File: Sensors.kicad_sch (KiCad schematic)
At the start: 17 parts, among them Q1 TEMT6000X01, U2 BME280, U7 MAX4466EXK

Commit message: setup net classes and started layout
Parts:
- C15, C16, C18, C20: footprint (none) -> Capacitor_SMD:C_0805_2012Metric
- R23, R24, R25, R26, R27, R28, R29, R30, R31: footprint (none) -> Resistor_SMD:R_0805_2012Metric
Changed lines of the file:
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@@
 			)
 		)
-		(property "Footprint" ""
+		(property "Footprint" "Resistor_SMD:R_0805_2012Metric"
 			(at 176.022 109.22 90)
 			(hide yes)
@@
 			)
 		)
-		(property "Footprint" ""
+		(property "Footprint" "Capacitor_SMD:C_0805_2012Metric"
 			(at 227.33 151.4348 0)
 			(hide yes)
@@
 			)
 		)
-		(property "Footprint" ""
+		(property "Footprint" "Resistor_SMD:R_0805_2012Metric"
 			(at 223.52 144.018 90)
 			(hide yes)
@@
 			)
 		)
-		(property "Footprint" ""
+		(property "Footprint" "Resistor_SMD:R_0805_2012Metric"
 			(at 176.022 133.35 90)
 			(hide yes)
@@
 			)
 		)
-		(property "Footprint" ""
+		(property "Footprint" "Capacitor_SMD:C_0805_2012Metric"
 			(at 107.6452 53.34 0)
 			(hide yes)
@@
 			)
 		)
-		(property "Footprint" ""
+		(property "Footprint" "Resistor_SMD:R_0805_2012Metric"
 			(at 43.942 46.99 90)
 			(hide yes)
@@
 			)
 		)
-		(property "Footprint" ""
+		(property "Footprint" "Resistor_SMD:R_0805_2012Metric"
 			(at 188.722 133.35 90)
 			(hide yes)
@@
 			)
 		)
-		(property "Footprint" ""
+		(property "Footprint" "Capacitor_SMD:C_0805_2012Metric"
 			(at 272.7452 115.57 0)
 			(hide yes)
@@
 			)
 		)
-		(property "Footprint" ""
+		(property "Footprint" "Resistor_SMD:R_0805_2012Metric"
 			(at 201.422 44.45 90)
 			(hide yes)
@@
 			)
 		)
-		(property "Footprint" ""
+		(property "Footprint" "Resistor_SMD:R_0805_2012Metric"
 			(at 33.782 46.99 90)
 			(hide yes)
@@
 			)
 		)
-		(property "Footprint" ""
+		(property "Footprint" "Resistor_SMD:R_0805_2012Metric"
 			(at 155.702 114.3 90)
 			(hide yes)
@@
 			)
 		)
-		(property "Footprint" ""
+		(property "Footprint" "Capacitor_SMD:C_0805_2012Metric"
 			(at 151.13 105.7148 0)
 			(hide yes)
@@
 			)
 		)
-		(property "Footprint" ""
+		(property "Footprint" "Resistor_SMD:R_0805_2012Metric"
 			(at 155.702 100.33 90)
 			(hide yes)

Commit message: imported all footprints into layout
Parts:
- MK1: footprint CMC-5042PF-AC:CUI_CMC-5042PF-AC -> ESP32_project_Footprints:CUI_CMC-5042PF-AC; Availability In Stock -> (none); Package None -> (none); Price None -> (none)
- Q1: footprint TEMT6000X01:TRANS_TEMT6000X01 -> ESP32_project_Footprints:TRANS_TEMT6000X01; Availability In Stock -> (none); Package 1206 Vishay -> (none); Price None -> (none)
- U2: footprint BME280:PSON65P250X250X100-8N -> ESP32_project_Footprints:PSON65P250X250X100-8N; Availability In Stock -> (none); Package LGA-8 Bosch -> (none); Price None -> (none)
- U7: footprint MAX4466EXK:SOT65P210X110-5N -> ESP32_project_Footprints:SOT65P210X110-5N; Availability In Stock -> (none); Package SC-70-5 Maxim -> (none); Price None -> (none)
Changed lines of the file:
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@@
 			)
 		)
-		(property "Footprint" "TEMT6000X01:TRANS_TEMT6000X01"
+		(property "Footprint" "ESP32_project_Footprints:TRANS_TEMT6000X01"
 			(at 189.23 53.34 0)
 			(hide yes)
@@
 			)
 		)
-		(property "Package" "1206 Vishay"
-			(at 189.23 53.34 0)
-			(hide yes)
-			(show_name no)
-			(do_not_autoplace no)
-			(effects
-				(font
-					(size 1.27 1.27)
-				)
-				(justify bottom)
-			)
-		)
-		(property "Price" "None"
-			(at 189.23 53.34 0)
-			(hide yes)
-			(show_name no)
-			(do_not_autoplace no)
-			(effects
-				(font
-					(size 1.27 1.27)
-				)
-				(justify bottom)
-			)
-		)
 		(property "Check_prices" "https://www.snapeda.com/parts/TEMT6000X01/Vishay+Semiconductor+Opto+Division/view-part/?ref=eda"
 			(at 189.23 53.34 0)
@@
 		)
 		(property "MP" "TEMT6000X01"
-			(at 189.23 53.34 0)
-			(hide yes)
-			(show_name no)
-			(do_not_autoplace no)
-			(effects
-				(font
-					(size 1.27 1.27)
-				)
-				(justify bottom)
-			)
-		)
-		(property "Availability" "In Stock"
 			(at 189.23 53.34 0)
 			(hide yes)
@@
 			)
 		)
-		(property "Footprint" "CMC-5042PF-AC:CUI_CMC-5042PF-AC"
+		(property "Footprint" "ESP32_project_Footprints:CUI_CMC-5042PF-AC"
 			(at 142.24 125.73 0)
 			(hide yes)
@@
 			)
 		)
-		(property "Package" "None"
-			(at 142.24 125.73 0)
-			(hide yes)
-			(show_name no)
-			(do_not_autoplace no)
-			(effects
-				(font
-					(size 1.27 1.27)
-				)
-				(justify bottom)
-			)
-		)
-		(property "Price" "None"
-			(at 142.24 125.73 0)
-			(hide yes)
-			(show_name no)
-			(do_not_autoplace no)
-			(effects
-				(font
-					(size 1.27 1.27)
-				)
-				(justify bottom)
-			)
-		)
 		(property "Check_prices" "https://www.snapeda.com/parts/CMC-5042PF-AC/Same+Sky/view-part/?ref=eda"
 			(at 142.24 125.73 0)
@@
 			)
 		)
-		(property "Availability" "In Stock"
-			(at 142.24 125.73 0)
-			(hide yes)
-			(show_name no)
-			(do_not_autoplace no)
-			(effects
-				(font
-					(size 1.27 1.27)
-				)
-				(justify bottom)
-			)
-		)
 		(property "MANUFACTURER" "CUI INC"
 			(at 142.24 125.73 0)
@@
 				)
 				(justify bottom)
+			)
+		)
+		(property "Purpose" ""
+			(at 142.24 125.73 0)
+			(show_name no)
+			(do_not_autoplace no)
+			(effects
+				(font
+					(size 1.27 1.27)
+				)
 			)
 		)
@@
 			)
 		)
-		(property "Footprint" "MAX4466EXK:SOT65P210X110-5N"
+		(property "Footprint" "ESP32_project_Footprints:SOT65P210X110-5N"
 			(at 226.06 121.92 0)
 			(hide yes)
@@
 			)
 		)
-		(property "Package" "SC-70-5 Maxim"
-			(at 226.06 121.92 0)
-			(hide yes)
-			(show_name no)
-			(do_not_autoplace no)
-			(effects
-				(font
-					(size 1.27 1.27)
-				)
-				(justify bottom)
-			)
-		)
-		(property "Price" "None"
-			(at 226.06 121.92 0)
-			(hide yes)
-			(show_name no)
-			(do_not_autoplace no)
-			(effects
-				(font
-					(size 1.27 1.27)
-				)
-				(justify bottom)
-			)
-		)
 		(property "SnapEDA_Link" "https://www.snapeda.com/parts/MAX4466EXK/Analog+Devices/view-part/?ref=snap"
 			(at 226.06 121.92 0)
@@
 		)
 		(property "MP" "MAX4466EXK"
-			(at 226.06 121.92 0)
-			(hide yes)
-			(show_name no)
-			(do_not_autoplace no)
-			(effects
-				(font
-					(size 1.27 1.27)
-				)
-				(justify bottom)
-			)
-		)
-		(property "Availability" "In Stock"
 			(at 226.06 121.92 0)
 			(hide yes)
@@
 			)
 		)
-		(property "Footprint" "BME280:PSON65P250X250X100-8N"
+		(property "Footprint" "ESP32_project_Footprints:PSON65P250X250X100-8N"
 			(at 76.2 57.15 0)
 			(hide yes)
@@
 			)
 		)
-		(property "Package" "LGA-8 Bosch"
-			(at 76.2 57.15 0)
-			(hide yes)
-			(show_name no)
-			(do_not_autoplace no)
-			(effects
-				(font
-					(size 1.27 1.27)
-				)
-				(justify bottom)
-			)
-		)
 		(property "Check_prices" "https://www.snapeda.com/parts/BME280/Bosch+Sensortec/view-part/?ref=eda"
 			(at 76.2 57.15 0)
@@
 			(at 76.2 57.15 0)
 			(hide yes)
-			(show_name no)
-			(do_not_autoplace no)
-			(effects
-				(font
-					(size 1.27 1.27)
-				)
-				(justify bottom)
-			)
-		)
-		(property "Price" "None"
-			(at 76.2 57.15 0)
-			(hide yes)
-			(show_name no)
-			(do_not_autoplace no)
-			(effects
-				(font
-					(size 1.27 1.27)
-				)
-				(justify bottom)
-			)
-		)
-		(property "Availability" "In Stock"
-			(at 76.2 57.15 0)
-			(hide yes)

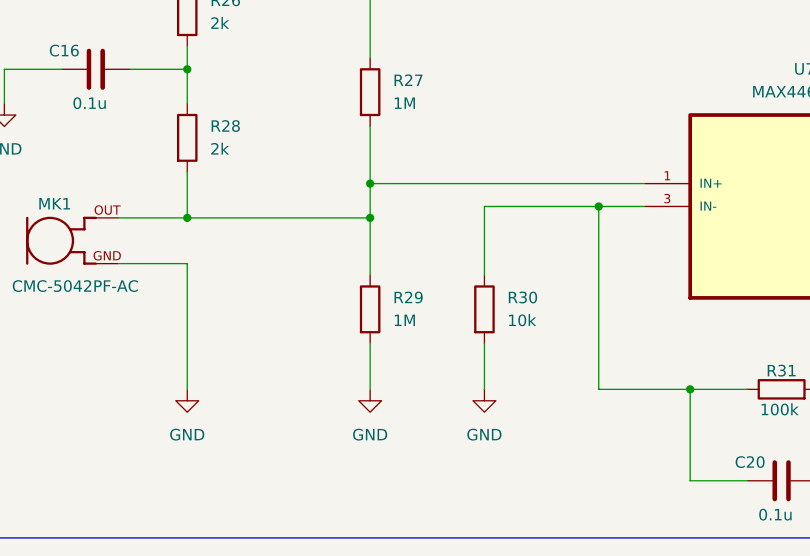
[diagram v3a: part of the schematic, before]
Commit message: finalized edge cuts and component placement
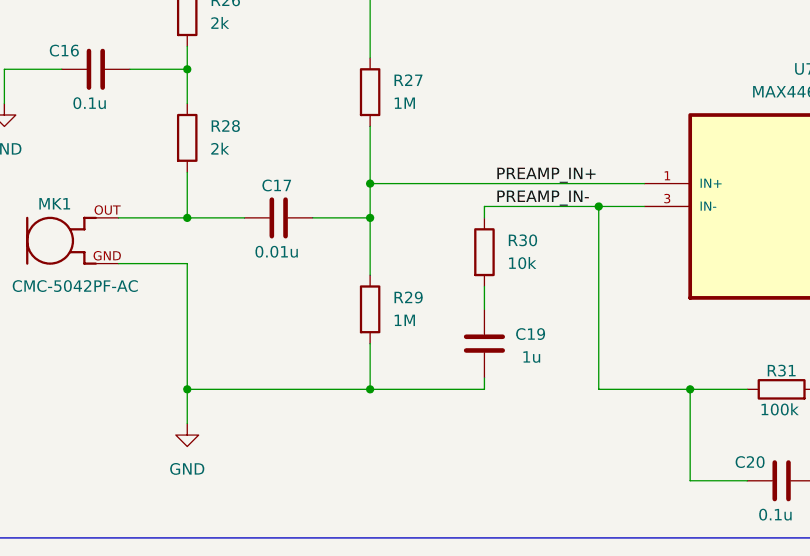
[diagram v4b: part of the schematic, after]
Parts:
- added C17: 0.01u, Capacitor_SMD:C_0805_2012Metric, symbol Device:C
- added C19: 1u, Capacitor_SMD:C_0805_2012Metric, symbol Device:C
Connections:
- net GND: now also C19.1; no longer R30.2
- net PREAMP_IN+: now reaches R27.2, R29.1, U7.1 (IN+)
- net PREAMP_IN+: now also C17.2; no longer MK1.OUT, R28.2
- net PREAMP_IN-: now reaches C20.1, R30.1, R31.1, U7.3 (IN-)
- new net: C17.1, MK1.OUT, R28.2
- new net: C19.2, R30.2
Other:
- moved on the sheet: R30

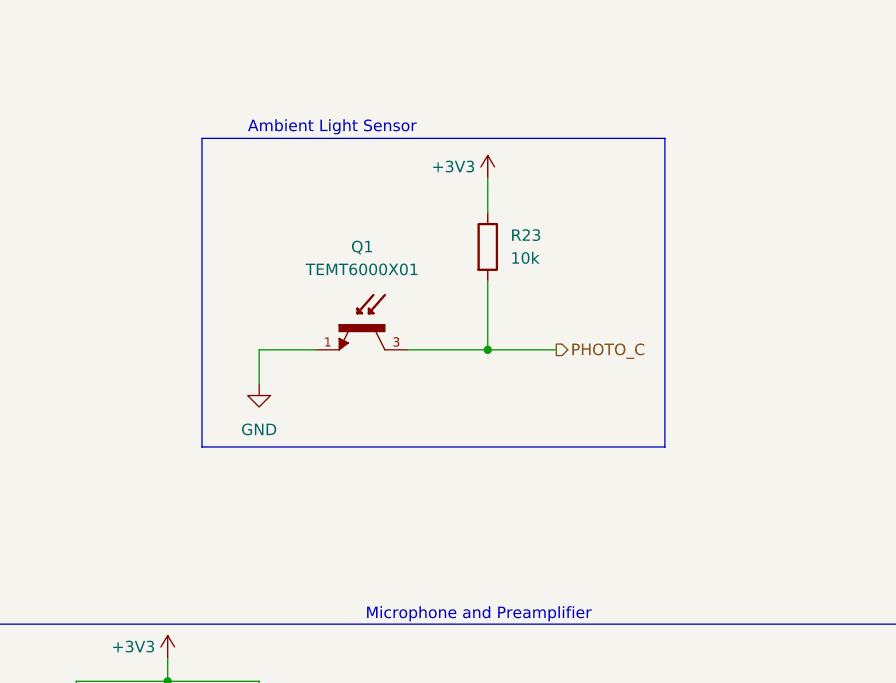
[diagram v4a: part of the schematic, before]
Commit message: corrected boot control schematic and layout
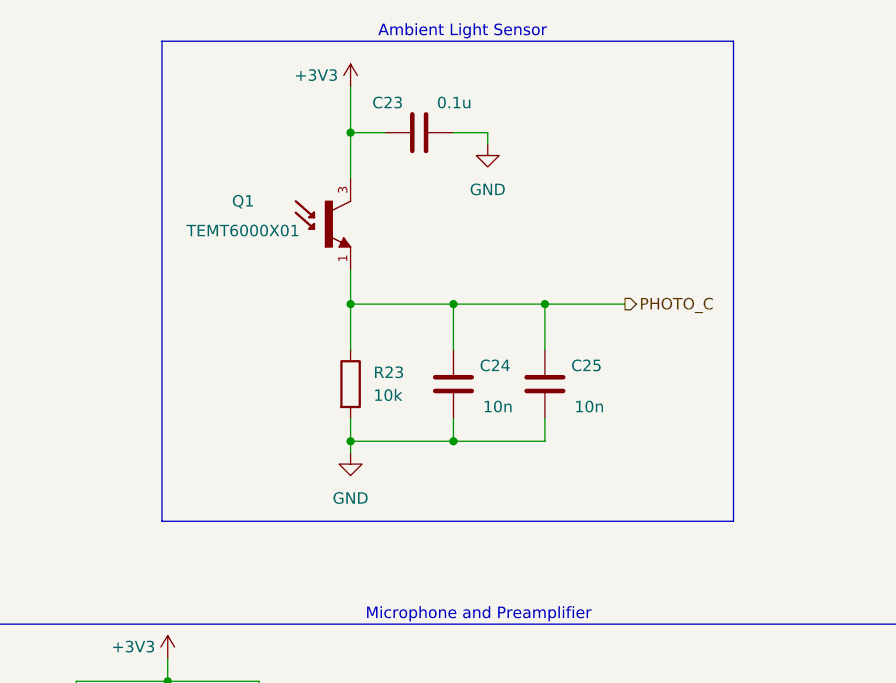
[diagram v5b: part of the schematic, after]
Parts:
- added C23: 0.1u, Capacitor_SMD:C_0805_2012Metric, symbol Device:C
- added C24, C25: 10n, Capacitor_SMD:C_0805_2012Metric, symbol Device:C
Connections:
- net +3V3: now also Q1.3, C23.1; no longer R23.1
- net GND: now also R23.2, C23.2, C24.1, C25.1; no longer Q1.1
- net PHOTO_C: now also Q1.1, R23.1, C24.2, C25.2; no longer Q1.3, R23.2
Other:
- moved on the sheet: Q1, R23

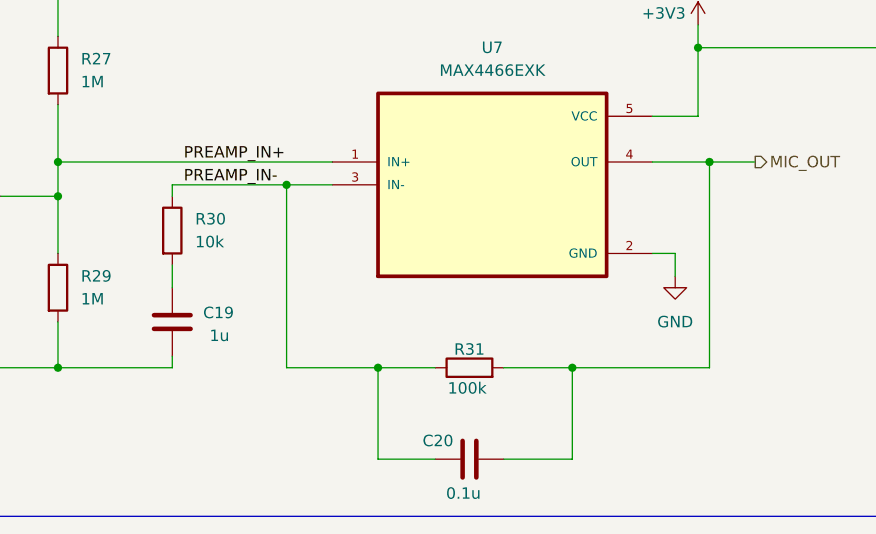
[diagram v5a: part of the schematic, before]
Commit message: added pot to mic amp, made buttons bigger
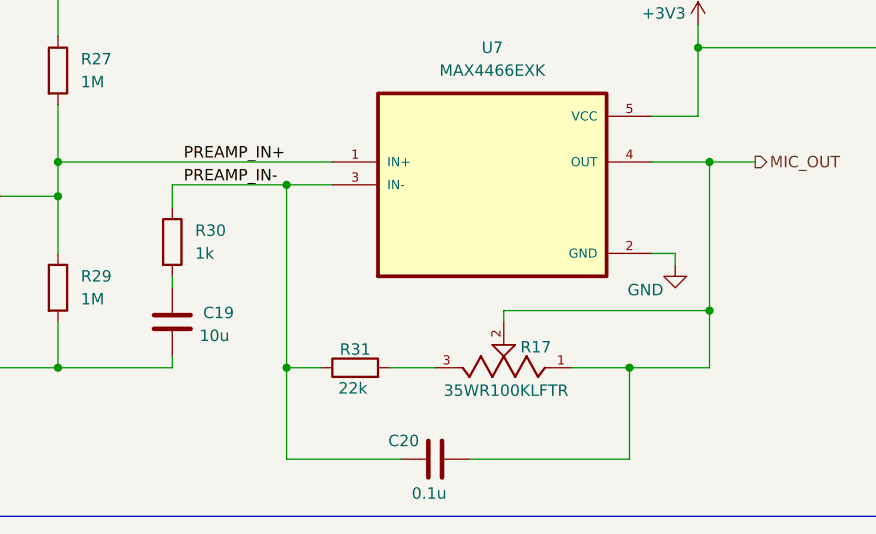
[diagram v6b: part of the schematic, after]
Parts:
- added R17: 35WR100KLFTR, ESP32_project_Footprints:TRIM_35WR100KLFTR, symbol 35WR100KLFTR:35WR100KLFTR
- C19: value 1u -> 10u
- R30: value 10k -> 1k
- R31: value 100k -> 22k
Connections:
- net MIC_OUT: now also R17.1, R17.2; no longer R31.2
- new net: R17.3, R31.2
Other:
- moved on the sheet: C20, R30, R31
